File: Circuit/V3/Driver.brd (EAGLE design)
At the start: 61 x 56 mm, 36 parts

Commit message: Change the orginal motor gate driver(DRV8305) to DRV8303 in schematic
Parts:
- removed C16: 1uF, rcl:C0603
- removed C4: 1nF, SparkFun-Capacitors:0603
- removed LED1, LED2: (no value), led:CHIPLED_0805
- removed R5: (no value), rcl:R2512
- removed U$3: DRV8305, BLDC project:PFB_S-PQFP-G48
- added C8: 2.2uF, SparkFun-Capacitors:0603
- added C9: 0.22uF, SparkFun-Capacitors:0603
- added IC1: DRV8303DCA, DRV8303DCA:SOP50P810X120-49N
- C1, C15: value 1uF -> 0.1uF; device rcl:C0603 -> SparkFun-Capacitors:0603
- C10: value 1uF -> 1.0uF; device rcl:C0603 -> SparkFun-Capacitors:0603
- C11: value 2.2uF -> 1.0uF; device rcl:C0603 -> SparkFun-Capacitors:0603
- C12: value 4.7uF -> 0.1uF; device rcl:C0603 -> SparkFun-Capacitors:0603
- C13: value 47nF -> 0.1uF; device rcl:C0603 -> SparkFun-Capacitors:0603
- C14: value 47nF -> 4.7uF; device rcl:C0603 -> SparkFun-Capacitors:0603
- R3: value 10k -> 1; device rcl:R0603 -> SparkFun-Resistors:0603
- R4: value 100 -> 10k; device rcl:R0603 -> SparkFun-Resistors:0603
- moved C15 84.5 mm to (1.00, -41.5), flipped to the top, turned to 0 degrees
- moved C14 79.9 mm to (1.00, -38.0), flipped to the top, turned to 0 degrees
- moved C13 78.6 mm to (1.00, -34.5), flipped to the top, turned to 0 degrees
- moved C12 77.0 mm to (1.00, -31.0), flipped to the top, turned to 0 degrees
- moved C11 73.0 mm to (1.00, -27.5), flipped to the top, turned to 0 degrees
- moved C10 71.7 mm to (1.00, -24.0), flipped to the top, turned to 0 degrees
- moved R4 54.6 mm to (1.00, -10.0), flipped to the top, turned to 0 degrees
- moved R6 35.7 mm to (1.00, -13.5), flipped to the top, turned to 0 degrees
- moved R3 31.5 mm to (1.00, -6.50), flipped to the top, turned to 0 degrees
- moved C1 30.1 mm to (1.00, -3.00), flipped to the top, turned to 0 degrees
- moved A 2.50 mm to (5.94, 2.20)
- moved B 2.50 mm to (13.6, 2.20)
- moved C 2.50 mm to (21.2, 2.20)
- moved TP2 1.00 mm to (29.1, 5.59)
- moved TP1 0.50 mm to (33.4, 5.59)
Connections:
- removed net CP1H: C14.2, U$3.43
- removed net CP1L: C14.1, U$3.42
- removed net CP2H: C13.1, U$3.39
- removed net CP2L: C13.2, U$3.40
- removed net DVDD: C15.1, U$3.46
- removed net N$15: C1.1, U$3.15
- removed net PWRGD: R3.2, U$3.13
- removed net SN3: C4.2, LC.2, R5.2, U$3.19, U$3.26
- removed net VCPH: C11.2, U$3.38
- removed net VCP_LSD: C10.1, U$3.37
- removed net VDRAIN: R4.1, U$3.44
- new net N$14: C13.1, IC1.34
- new net N$2: C1.1, IC1.44
- new net N$26: IC1.3, R3.2
- new net N$32: C8.1, IC1.9
- new net N$33: C9.2, IC1.10
- new net N$34: C9.1, IC1.11
- new net N$43: C10.2, IC1.19
- new net N$47: C11.1, IC1.23
- new net N$9: C12.1, IC1.39
- net GH_A: now also IC1.43; no longer U$3.36
- net GH_B: now also IC1.38; no longer U$3.29
- net GH_C: now also IC1.33; no longer U$3.28
- net GL_A: now also IC1.41; no longer U$3.33
- net GL_B: now also IC1.36; no longer U$3.32
- net GL_C: now also IC1.31; no longer U$3.25
- net GND: now also C10.1, C11.2, C14.2, C8.2, IC1.24, IC1.26, IC1.28, IC1.30, IC1.46, IC1.47, IC1.48, IC1.49, LC.2, R3.1; no longer C1.2, C10.2, C12.2, C16.2, C4.1, LED1.C, LED2.C, R5.1, U$3.14, U$3.20, U$3.22, U$3.24, U$3.45, U$3.P$1, U$3.P$10, U$3.P$11, U$3.P$12, U$3.P$13, U$3.P$14, U$3.P$15, U$3.P$16, U$3.P$17, U$3.P$18, U$3.P$19, U$3.P$2, U$3.P$20, U$3.P$21, U$3.P$22, U$3.P$23, U$3.P$24, U$3.P$25, U$3.P$26, U$3.P$27, U$3.P$3, U$3.P$4, U$3.P$5, U$3.P$6, U$3.P$7, U$3.P$8, U$3.P$9
- net PA10: now also IC1.15; no longer U$3.4
- net PA3: no longer U$3.18
- net PA4: now also IC1.4; no longer U$3.9
- net PA5: now also IC1.7; no longer U$3.12
- net PA6: now also IC1.6; no longer U$3.11
- net PA7: now also IC1.5; no longer U$3.10
- net PA8: now also IC1.13; no longer U$3.2
- net PA9: now also IC1.14; no longer U$3.3
- net PB0: now also IC1.22; no longer U$3.17
- net PB1: now also IC1.21; no longer U$3.16
- net PB12: now also IC1.12; no longer LED2.A, U$3.1
- net PB13: now also IC1.2, R6.1
- net PB14: now also IC1.1, R4.1
- net PB4: now also IC1.8
- net PB6: now also IC1.16; no longer U$3.5
- net PB7: now also IC1.17; no longer U$3.6
- net PB8: now also IC1.18; no longer U$3.7
- net PB9: no longer LED1.A, R6.2, U$3.8
- net SH_A: now also C1.2, IC1.42; no longer U$3.35
- net SH_B: now also C12.2, IC1.37; no longer U$3.30
- net SH_C: now also C13.2, IC1.32; no longer U$3.27
- net SN1: now also IC1.29, IC1.40; no longer U$3.23, U$3.34
- net SN2: now also IC1.27, IC1.35; no longer U$3.21, U$3.31
- net VCC: now also C14.1, C15.1, IC1.20, IC1.25, IC1.45, R4.2, R6.2; no longer C16.1, R3.1, R6.1, U$3.48
- net VIN: no longer C11.1, C12.1, R4.2, U$3.41
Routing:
- net GND: track 274.0 -> 38.5 mm, vias 4 -> 0
- net PB9: track 122.2 -> 0.00 mm, vias 2 -> 0
- net VCC: track 93.7 -> 0.00 mm, vias 2 -> 0
- net GL_C: track 85.3 -> 0.00 mm, vias 1 -> 0
- net SN1: track 78.0 -> 0.00 mm, vias 13 -> 9
- net SN2: track 75.6 -> 0.00 mm, vias 13 -> 9
- net N$15: track 72.5 -> 0.00 mm, vias 4 -> 0
- net PB12: track 60.3 -> 0.00 mm, vias 1 -> 0
- net PWRGD: track 58.1 -> 0.00 mm, vias 2 -> 0
- net GL_A: track 57.0 -> 0.00 mm, vias 1 -> 0
- net GL_B: track 43.0 -> 0.00 mm, vias 3 -> 0
- net SH_A: track 57.9 -> 18.5 mm, vias 3 -> 0
- net VCP_LSD: track 36.4 -> 0.00 mm, vias 2 -> 0
- net VIN: track 91.0 -> 56.2 mm, vias 2 -> 0
- net PA8: track 33.3 -> 0.00 mm, vias 1 -> 0
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- added copper zone on layer 1, net GND
- removed copper zone on layer 1, net SN3
- removed copper zone on layer 16, net SN3
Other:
- board text added: "DRV8303"
- board text added: "V3"
- board text removed: "DRV8305"
- board text removed: "V2"

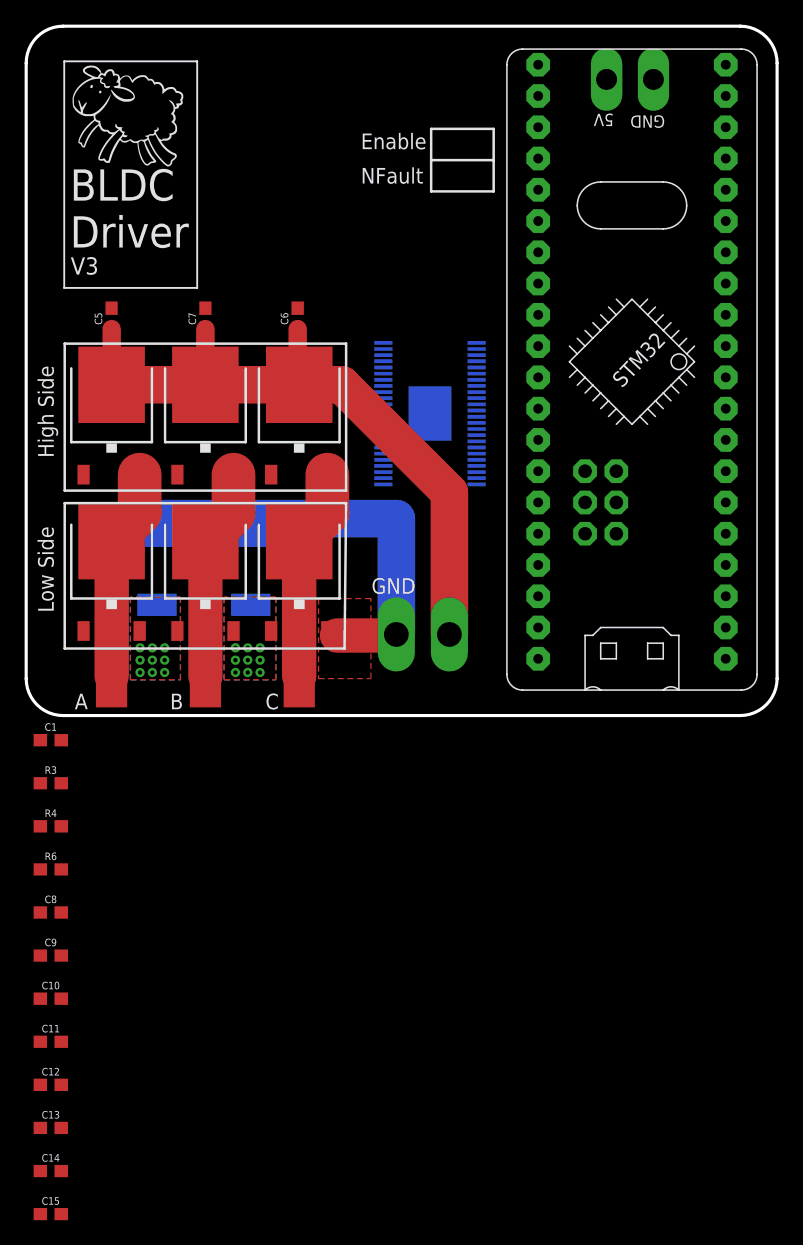
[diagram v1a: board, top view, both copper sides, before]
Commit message: Routing the basic circuit and route. A backup before autorouting
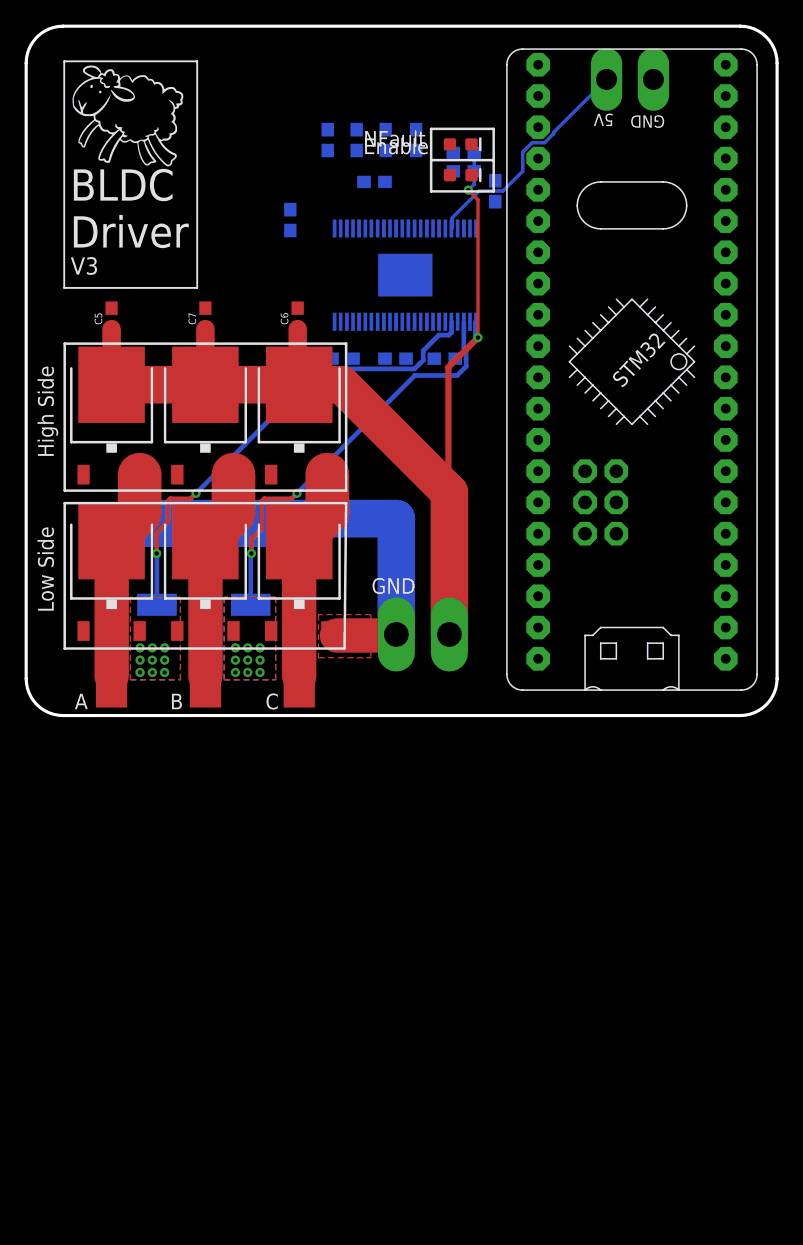
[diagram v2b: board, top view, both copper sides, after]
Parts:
- added D1, D2: BLUE, SparkFun-LED:LED-0603
- moved C15 92.5 mm to (34.5, 44.7), flipped to the bottom
- moved C14 87.9 mm to (34.5, 43.2), flipped to the bottom
- moved C11 78.0 mm to (37.1, 41.6), flipped to the bottom, turned to 90 degrees
- moved C10 75.8 mm to (30.7, 45.8), flipped to the bottom, turned to 270 degrees
- moved C13 70.2 mm to (33.0, 28.0), flipped to the bottom, turned to 180 degrees
- moved C8 68.4 mm to (28.2, 45.8), flipped to the bottom, turned to 90 degrees
- moved C9 68.1 mm to (27.3, 42.4), flipped to the bottom
- moved C12 65.3 mm to (29.0, 28.0), flipped to the bottom, turned to 180 degrees
- moved R6 64.3 mm to (25.9, 45.8), flipped to the bottom, turned to 90 degrees
- moved R4 60.1 mm to (23.5, 45.8), flipped to the bottom, turned to 90 degrees
- moved R3 49.7 mm to (20.4, 39.2), flipped to the bottom, turned to 270 degrees
- moved C1 39.0 mm to (24.7, 28.0), flipped to the bottom, turned to 180 degrees
- moved IC1 11.4 mm to (29.8, 34.8), turned to 270 degrees
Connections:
- net GND: now also D1.C, D2.C
- net PB12: now also D2.A
- net PB13: now also D1.A
- net VCC: no longer C14.1, C15.1, IC1.25
- net VIN: now also C14.1, C15.1, IC1.25
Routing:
- net VIN: track 56.2 -> 98.7 mm, vias 0 -> 2
- net SN1: track 0.00 -> 38.8 mm, vias 9 -> 11
- net SN2: track 0.00 -> 33.6 mm, vias 9 -> 11
- net VCC: track 0.00 -> 19.1 mm
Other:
- board text removed: "DRV8303"

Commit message: Fixed some bugs and edited the note.md
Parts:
- removed R3: 1, SparkFun-Resistors:0603
- added C16: 2.2nF, SparkFun-Capacitors:0603
- added R5, R7: 0, SparkFun-Resistors:0603
- moved 5V 46.3 mm to (48.1, 4.37)
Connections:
- removed net N$26: IC1.3, R3.2
- new net N$1: IC1.21, R5.2
- net GND: now also C16.2, IC1.3; no longer R3.1
- net N$3: now also IC1.22, R7.2; no longer U$1.P$23
- net PB0: now also C16.1, R7.1; no longer IC1.22
- net PB1: now also R5.1; no longer IC1.21
- net VCC: now also U$1.P$23; no longer U$1.P$18
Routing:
- net VCC: track 19.1 -> 5.90 mm

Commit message: Fixed some bugs
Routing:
- net GND: track 38.5 -> 66.9 mm
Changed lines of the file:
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@@
 <contactref element="IC1" pad="30"/>
 <wire x1="29.07" y1="5.588" x2="29.07" y2="15" width="3.048" layer="16"/>
-<wire x1="29.07" y1="15" x2="17" y2="15" width="3.048" layer="16"/>
+<wire x1="29.07" y1="15" x2="27.25" y2="15" width="3.048" layer="16"/>
+<wire x1="27.25" y1="15" x2="17" y2="15" width="3.048" layer="16"/>
 <wire x1="17" y1="15" x2="9.5" y2="15" width="3.048" layer="16"/>
 <wire x1="8" y1="15" x2="9.5" y2="15" width="3.048" layer="16"/>
@@
 <contactref element="C16" pad="2"/>
 <contactref element="IC1" pad="3"/>
+<wire x1="34.82525625" y1="32.0289" x2="34.27474375" y2="32.0289" width="0.3" layer="16"/>
+<wire x1="35.05" y1="30.989" x2="35.0429" y2="30.9961" width="0.3" layer="16"/>
+<wire x1="34.0571" y1="30.9961" x2="34.05" y2="30.989" width="0.3" layer="16"/>
+<wire x1="35.0429" y1="30.9961" x2="35.0429" y2="31.81125625" width="0.3" layer="16"/>
+<wire x1="35.0429" y1="31.81125625" x2="34.82525625" y2="32.0289" width="0.3" layer="16"/>
+<wire x1="34.27474375" y1="32.0289" x2="34.0571" y2="31.81125625" width="0.3" layer="16"/>
+<wire x1="34.0571" y1="31.81125625" x2="34.0571" y2="30.9961" width="0.3" layer="16"/>
+<wire x1="33.82525625" y1="32.0289" x2="33.27474375" y2="32.0289" width="0.3" layer="16"/>
+<wire x1="34.05" y1="30.989" x2="34.0429" y2="30.9961" width="0.3" layer="16"/>
+<wire x1="33.0571" y1="30.9961" x2="33.05" y2="30.989" width="0.3" layer="16"/>
+<wire x1="34.0429" y1="30.9961" x2="34.0429" y2="31.81125625" width="0.3" layer="16"/>
+<wire x1="34.0429" y1="31.81125625" x2="33.82525625" y2="32.0289" width="0.3" layer="16"/>
+<wire x1="33.27474375" y1="32.0289" x2="33.0571" y2="31.81125625" width="0.3" layer="16"/>
+<wire x1="33.0571" y1="31.81125625" x2="33.0571" y2="30.9961" width="0.3" layer="16"/>
+<wire x1="35.27474375" y1="32.0289" x2="35.82525625" y2="32.0289" width="0.3" layer="16"/>
+<wire x1="34.1976" y1="22.95225625" x2="34.1976" y2="21.9476" width="0.3" layer="16"/>
+<wire x1="34.1976" y1="21.9476" x2="27.25" y2="15" width="0.3" layer="16"/>
+<wire x1="35.0576" y1="31.81175625" x2="35.27474375" y2="32.0289" width="0.3" layer="16"/>
+<wire x1="35.2358" y1="23.99045625" x2="34.1976" y2="22.95225625" width="0.3" layer="16"/>
+<wire x1="35.82525625" y1="32.0289" x2="36.3806" y2="31.47355625" width="0.3" layer="16"/>
+<wire x1="36.3806" y1="31.47355625" x2="36.3806" y2="29.41808125" width="0.3" layer="16"/>
+<wire x1="35.05" y1="30.989" x2="35.0576" y2="30.9966" width="0.3" layer="16"/>
+<wire x1="35.0576" y1="30.9966" x2="35.0576" y2="31.81175625" width="0.3" layer="16"/>
+<wire x1="35.2358" y1="28.27328125" x2="35.2358" y2="23.99045625" width="0.3" layer="16"/>
+<wire x1="36.3806" y1="29.41808125" x2="35.2358" y2="28.27328125" width="0.3" layer="16"/>
 <wire x1="37.1" y1="42.45" x2="55.831" y2="49.33" width="0" layer="19" extent="16-16"/>
 <wire x1="35.177" y1="42.9" x2="37.1" y2="42.45" width="0" layer="19" extent="1-16"/>
@@
 <wire x1="29.8" y1="34.777" x2="35.55" y2="38.565" width="0" layer="19" extent="16-16"/>
 <wire x1="33.05" y1="30.989" x2="29.8" y2="34.777" width="0" layer="19" extent="16-16"/>
-<wire x1="34.05" y1="30.989" x2="33.05" y2="30.989" width="0" layer="19" extent="16-16"/>
-<wire x1="35.05" y1="30.989" x2="34.05" y2="30.989" width="0" layer="19" extent="16-16"/>
+<wire x1="23.46" y1="5.868" x2="24.25" y2="5.5" width="0" layer="19" extent="1-1"/>
+<wire x1="5.94" y1="11.518" x2="8" y2="15" width="0" layer="19" extent="16-16"/>
+<wire x1="13.56" y1="11.518" x2="17.243" y2="13.595" width="0" layer="19" extent="16-16"/>
 <wire x1="25.05" y1="38.565" x2="29.8" y2="34.777" width="0" layer="19" extent="16-16"/>
 <wire x1="25.05" y1="30.989" x2="29.8" y2="34.777" width="0" layer="19" extent="16-16"/>
@@
 <wire x1="13.56" y1="32.092" x2="21.053" y2="32.092" width="0" layer="19" extent="1-1"/>
 <wire x1="5.94" y1="32.092" x2="13.56" y2="32.092" width="0" layer="19" extent="1-1"/>
-<wire x1="8" y1="15" x2="5.94" y2="32.092" width="0" layer="19" extent="1-16"/>
-<wire x1="23.46" y1="5.868" x2="24.25" y2="5.5" width="0" layer="19" extent="1-1"/>
-<wire x1="5.94" y1="11.518" x2="8" y2="15" width="0" layer="19" extent="16-16"/>
-<wire x1="13.56" y1="11.518" x2="17.243" y2="13.595" width="0" layer="19" extent="16-16"/>
 <wire x1="40.591" y1="6.15" x2="29.07" y2="5.588" width="0" layer="19" extent="1-1"/>
 <wire x1="40.591" y1="3.61" x2="40.591" y2="6.15" width="0" layer="19" extent="1-1"/>
@@
 <contactref element="C14" pad="1"/>
 <contactref element="C15" pad="1"/>
-<wire x1="35.55" y1="30.989" x2="35.55" y2="29.85" width="0.5" layer="16"/>
-<wire x1="35.55" y1="29.85" x2="35.7" y2="29.7" width="0.5" layer="16"/>
 <via x="35.7" y="29.7" extent="1-16" drill="0.35"/>
 <wire x1="35.7" y1="29.7" x2="33.3" y2="27.3" width="0.5" layer="1"/>
@@
 <wire x1="34.917803125" y1="41.682196875" x2="35.7" y2="40.9" width="0.28" layer="1"/>
 <wire x1="35.7" y1="40.9" x2="35.7" y2="29.7" width="0.28" layer="1"/>
+<wire x1="35.55" y1="30.989" x2="35.55" y2="29.85" width="0.38" layer="16"/>
+<wire x1="35.55" y1="29.85" x2="35.7" y2="29.7" width="0.38" layer="16"/>
 <wire x1="33.38" y1="5.588" x2="33.3" y2="5.1" width="0" layer="19" extent="1-1"/>
 </signal>
@@
 <contactref element="IC1" pad="12"/>
 <contactref element="D2" pad="A"/>
-<wire x1="55.831" y1="3.61" x2="29.55" y2="38.565" width="0" layer="19" extent="16-16"/>
+<wire x1="29.55" y1="38.565" x2="55.831" y2="3.61" width="0" layer="19" extent="16-16"/>
 <wire x1="33.423" y1="42.9" x2="29.55" y2="38.565" width="0" layer="19" extent="1-16"/>
 </signal>
@@
 <mfgpreviewcolor name="substratecolor" color="0xFF786E46"/>
 </mfgpreviewcolors>
-<errors>
-</errors>
 </board>
 </drawing>

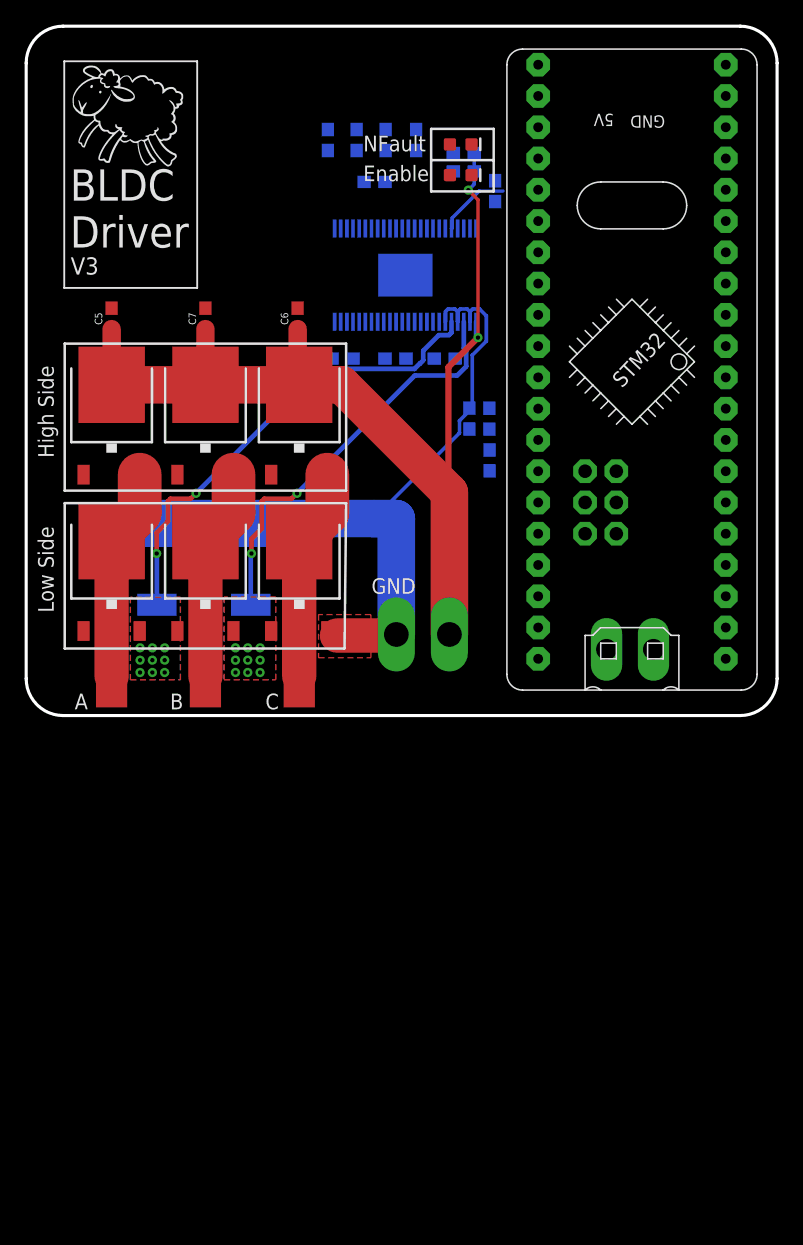
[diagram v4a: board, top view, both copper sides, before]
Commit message: autorouted the circuit
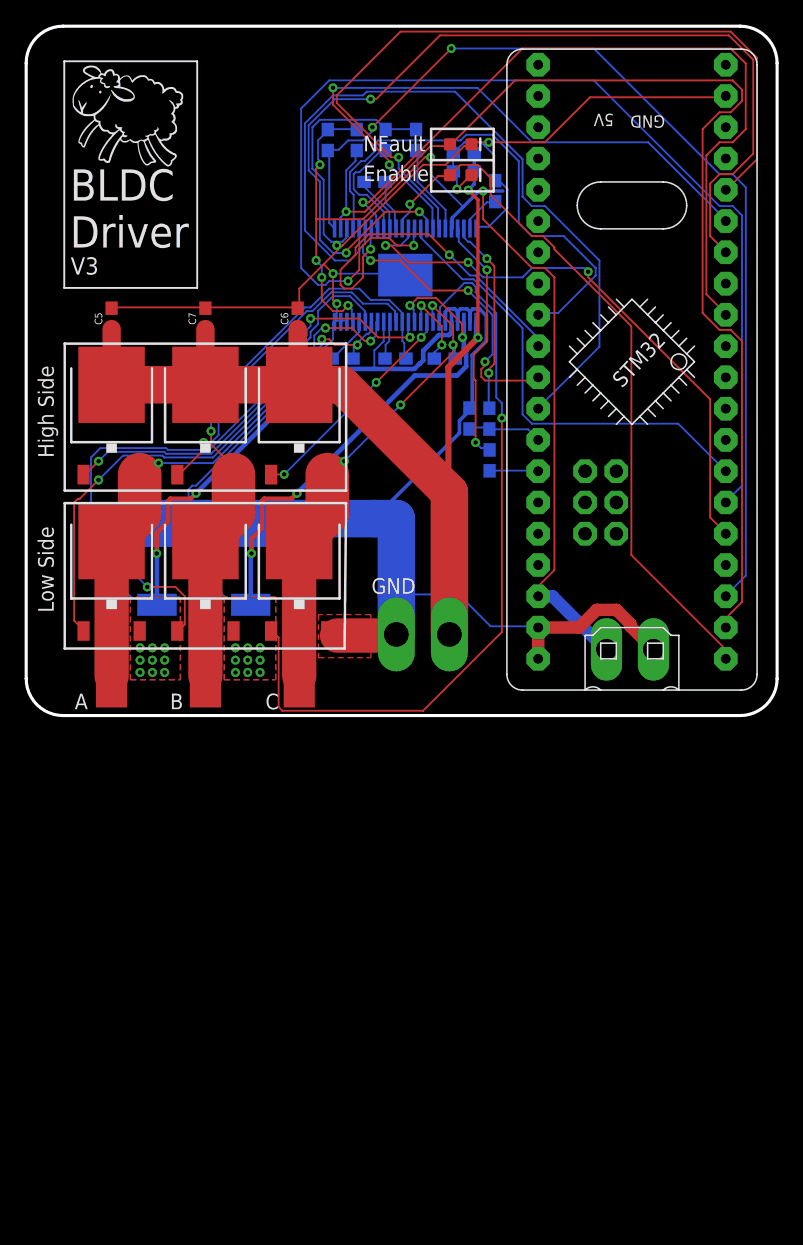
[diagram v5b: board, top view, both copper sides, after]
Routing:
- net GND: track 66.9 -> 232.6 mm, vias 0 -> 5
- net PA9: track 0.00 -> 92.1 mm, vias 0 -> 2
- net PB13: track 0.00 -> 91.8 mm, vias 0 -> 1
- net PB14: track 0.00 -> 82.7 mm, vias 0 -> 2
- net VCC: track 5.90 -> 87.3 mm, vias 0 -> 6
- net PB6: track 0.00 -> 79.5 mm, vias 0 -> 3
- net PB8: track 0.00 -> 63.6 mm, vias 0 -> 1
- net PA7: track 0.00 -> 62.8 mm
- net PB4: track 0.00 -> 62.4 mm, vias 0 -> 1
- net GL_C: track 0.00 -> 61.3 mm, vias 0 -> 1
- net PB12: track 0.00 -> 58.1 mm, vias 0 -> 1
- net GL_B: track 0.00 -> 54.3 mm, vias 0 -> 3
- net PB7: track 0.00 -> 51.2 mm, vias 0 -> 2
- net PA8: track 0.00 -> 46.7 mm, vias 0 -> 3
- net GL_A: track 0.00 -> 44.1 mm, vias 0 -> 3
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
